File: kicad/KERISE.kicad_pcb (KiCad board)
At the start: 2 copper layers, 40 x 44 mm, 91 parts, among them J1 Host, J2 Slave, J3 Host, J4 Slave, J5 COM, J6 Host, J7 Slave, J8 Host, J9 Slave, P1 Motor_L, P10 ENC_Slave, P2 Motor_R, P3 Battery, P4 Fan, P5 ENC_Host, P6 ENC_Slave, P7 ToF_Host, P8 ToF_Slave, P9 ENC_Host, Q1 DMN3065LW-7, Q2 SFH3015FA, Q3 DMN3065LW-7, Q4 SFH3015FA, Q5 DMN3065LW-7, Q6 DMN3065LW-7, Q7 SFH3015FA, Q8 DMN3065LW-7, Q9 SFH3015FA, SW1 SW_Push, SW2 SW_Push, U1 ESP32-PICO-D4, U10 LMV321, U2 DRV8835, U3 LXDC2UR30, U4 AS5048A, U5 VL6180X, U6 AS5048A, U7 ICM-20602, U8 ICM-20602, U9 PCA9632

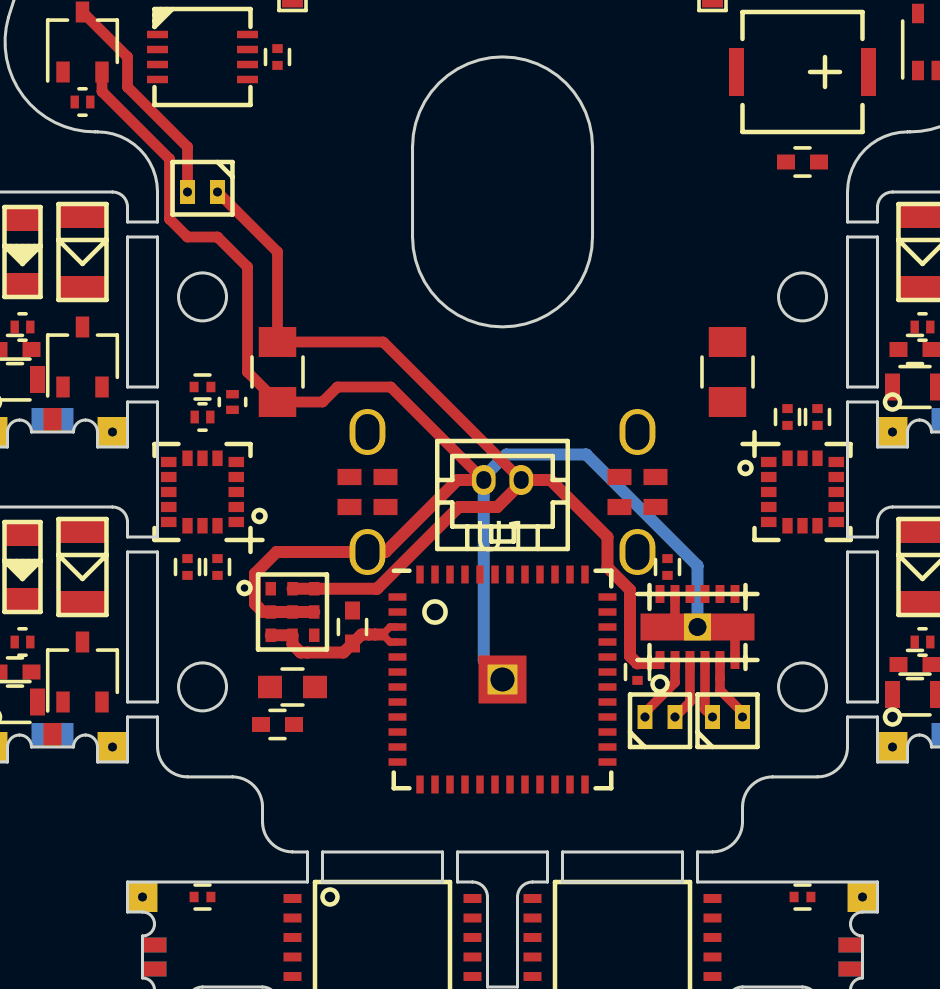
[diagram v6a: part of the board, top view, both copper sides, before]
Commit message: 電源回りの配線を改良
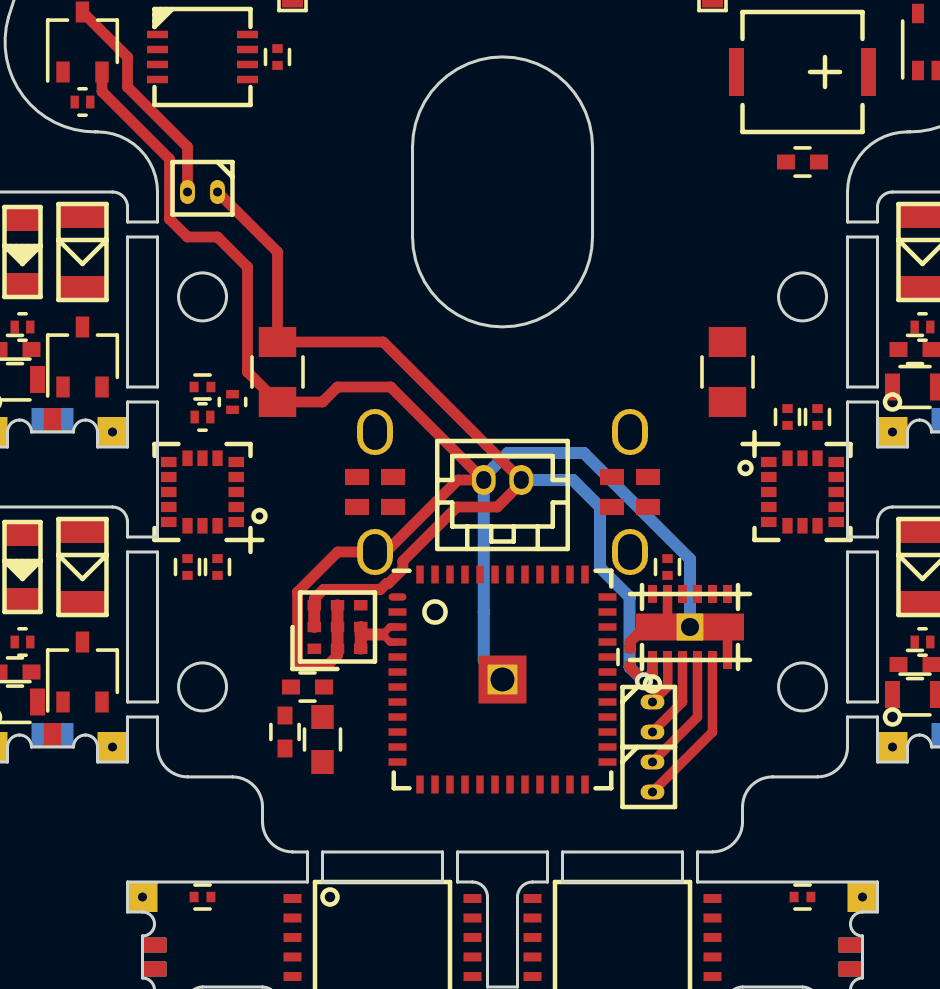
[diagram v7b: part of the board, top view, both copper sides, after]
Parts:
- moved P2 3.20 mm to (153.5, 122.5), turned to 270 degrees
- moved C1 2.50 mm to (142.0, 119.5), turned to 0 degrees
- moved L1 2.02 mm to (142.5, 121.2), turned to 90 degrees
- moved U3 1.58 mm to (143.0, 117.5), turned to 180 degrees
- moved C2 0.56 mm to (152.8, 118.5), turned to 90 degrees
- moved C7 0.35 mm to (141.2, 121.0), turned to 90 degrees
- moved P1 0.25 mm to (153.5, 120.5), turned to 270 degrees
- moved P5 0.25 mm to (144.2, 113.0)
- moved P9 0.25 mm to (152.8, 113.0)
- moved U2 0.25 mm to (154.8, 117.5)
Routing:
- net GND: track 57.6 -> 60.8 mm
- net /Motor/MT_OUT_R2: track 2.21 -> 5.23 mm
- net +3V3: track 5.60 -> 2.66 mm
- net +BATT: track 34.2 -> 36.9 mm, vias 0 -> 1
- net /Motor/MT_OUT_R1: track 2.00 -> 4.02 mm
- net /Motor/MT_OUT_L2: track 2.11 -> 2.81 mm
- net /Motor/MT_OUT_L1: track 2.32 -> 1.62 mm

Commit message: 自動配線成功
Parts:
- moved R12 0.79 mm to (161.8, 118.2), turned to 0 degrees
- moved R14 0.79 mm to (161.8, 107.8), turned to 0 degrees
- moved R7 0.79 mm to (131.8, 107.8), turned to 0 degrees
- moved R9 0.79 mm to (131.8, 118.2), turned to 0 degrees
- moved C16 0.25 mm to (162.2, 119.0)
- moved C17 0.25 mm to (162.2, 108.5)
- moved C8 0.25 mm to (132.2, 108.5)
- moved R11 0.25 mm to (162.2, 120.0)
- moved R6 0.25 mm to (132.2, 109.5)
